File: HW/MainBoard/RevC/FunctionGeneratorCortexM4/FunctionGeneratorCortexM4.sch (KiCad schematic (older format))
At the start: 2 parts, among them J1 Conn_02x05_Odd_Even, J2 Screw_Terminal_01x02

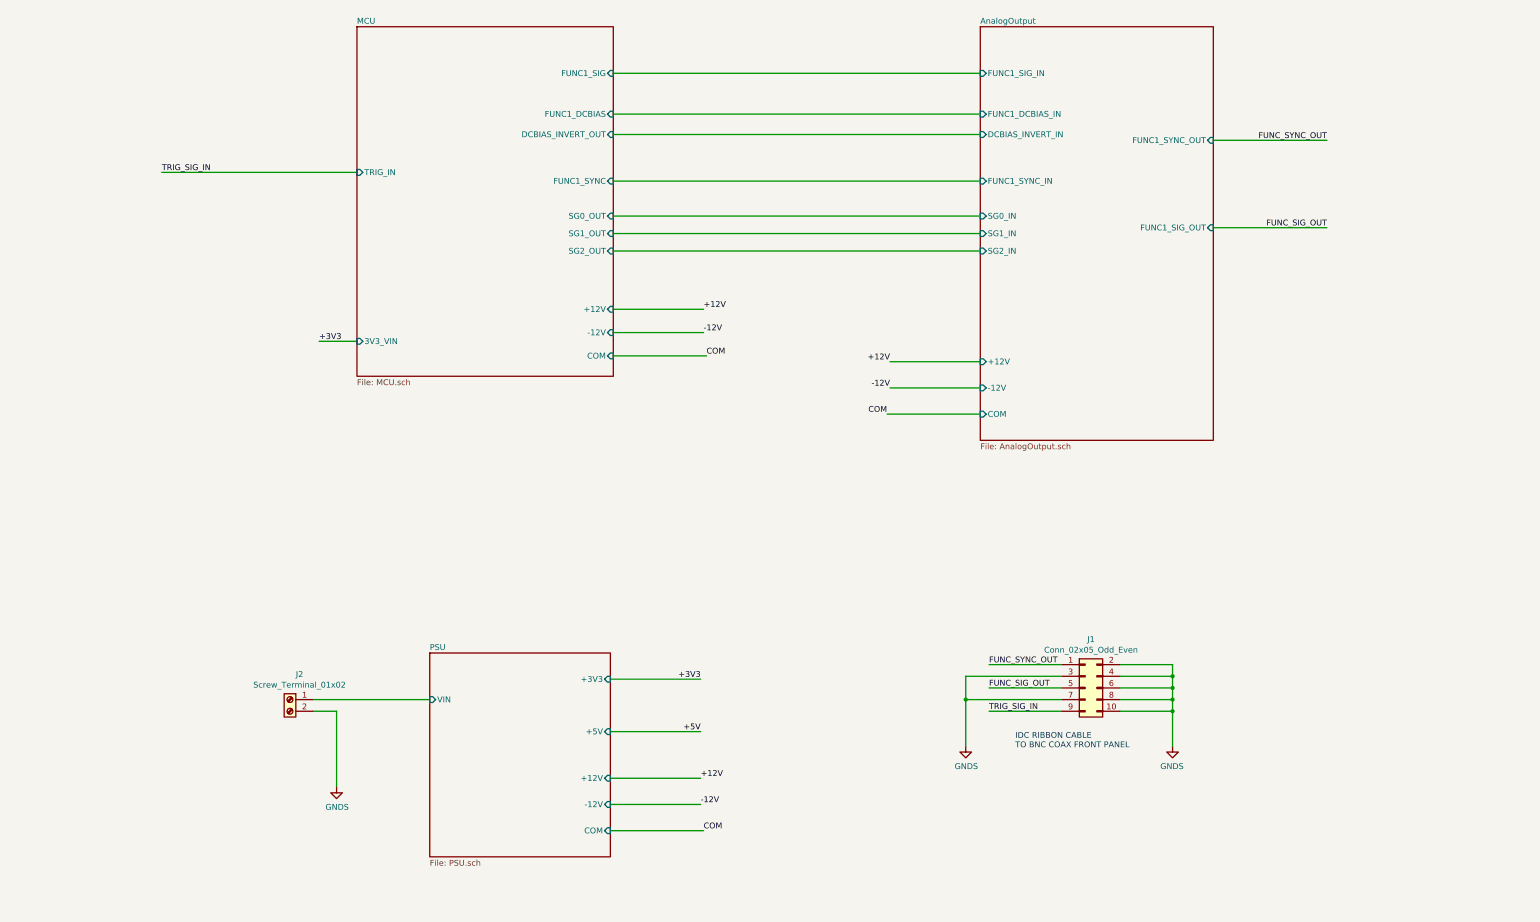
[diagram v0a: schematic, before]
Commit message: Updated MainBoard RevC
- Block diagram and connections completed on schematic
- Need to check MCU pin availability
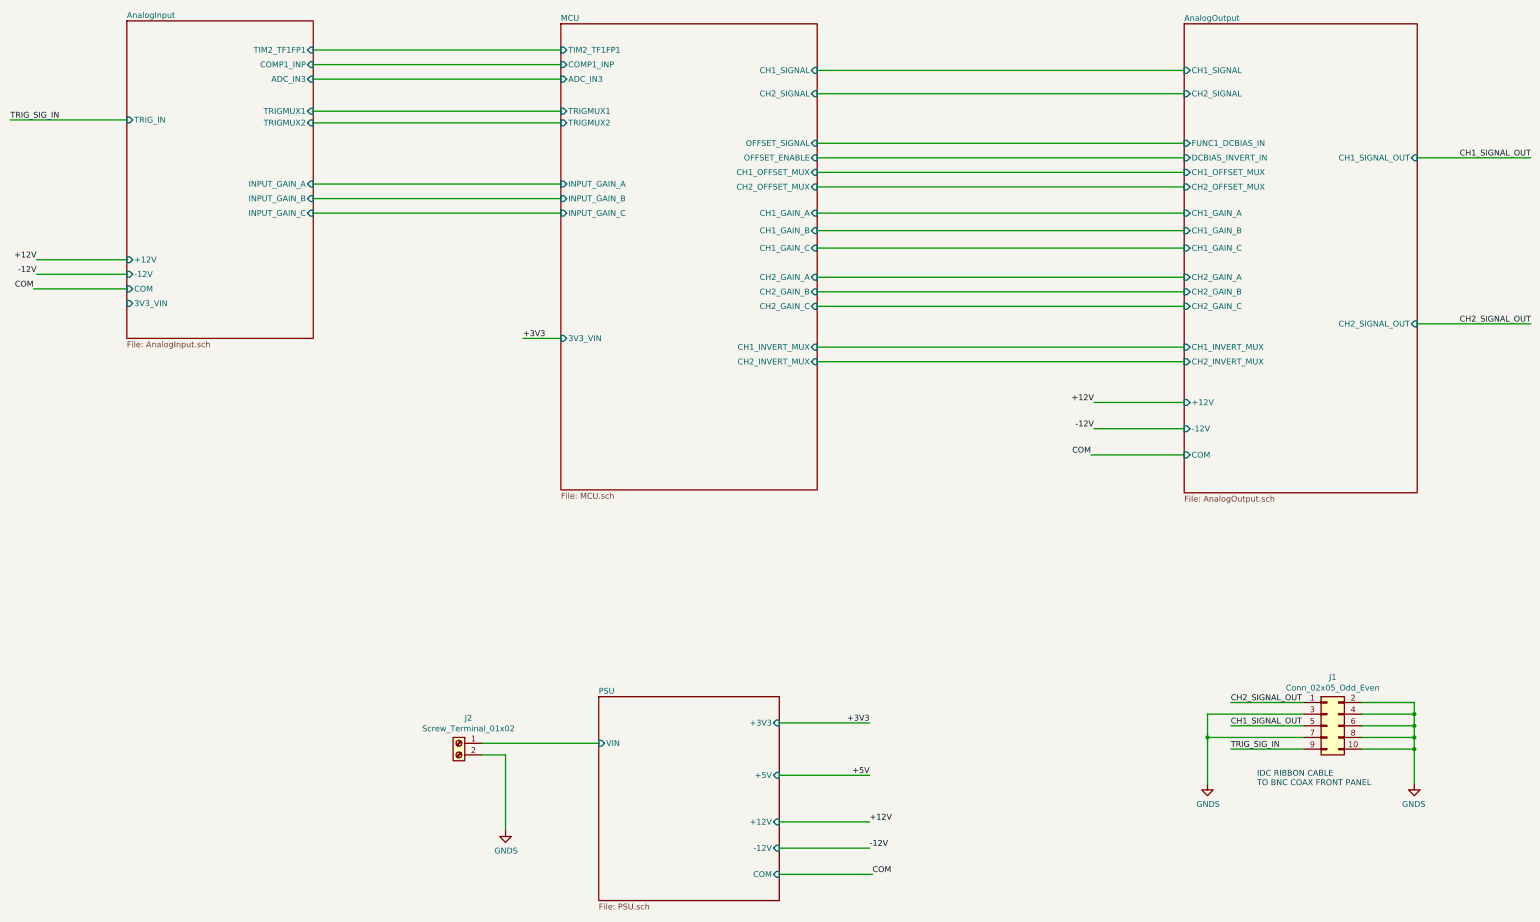
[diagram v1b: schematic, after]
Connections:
- net FUNC_SIG_OUT renamed CH1_SIGNAL_OUT
- net FUNC_SYNC_OUT renamed CH2_SIGNAL_OUT
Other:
- moved on the sheet: J1, J2

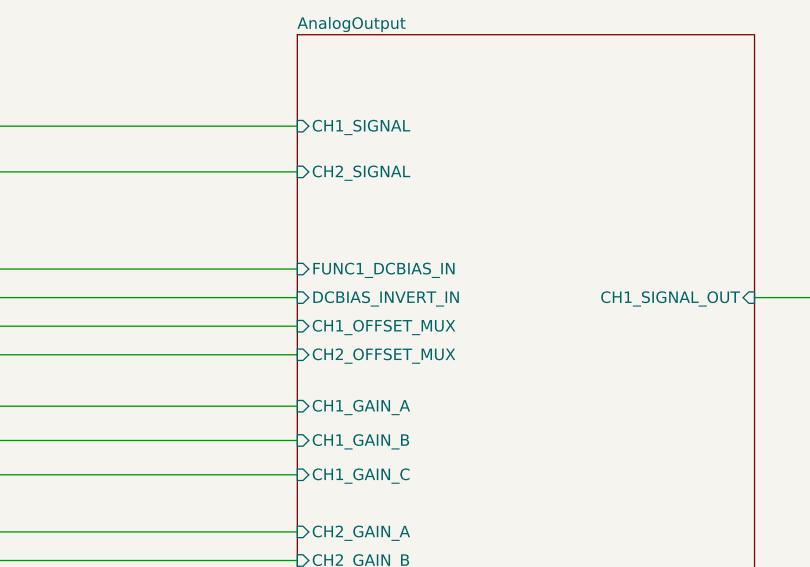
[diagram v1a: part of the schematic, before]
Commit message: Changed OFFSET SPDT to DG470
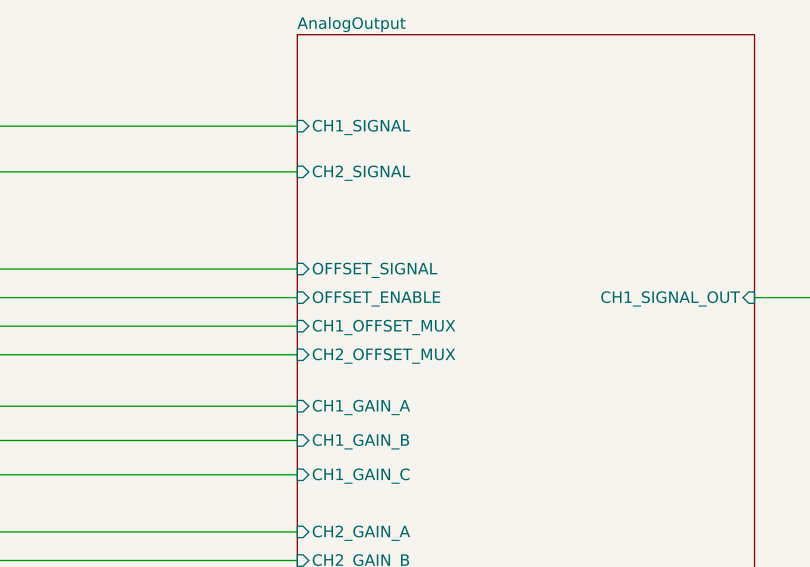
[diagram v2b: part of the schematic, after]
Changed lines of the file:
@@
 F0 "AnalogOutput" 50
 F1 "AnalogOutput.sch" 50
-F2 "FUNC1_DCBIAS_IN" I L 11600 2725 50
-F3 "DCBIAS_INVERT_IN" I L 11600 2850 50
-F4 "+12V" I L 11600 4950 50
-F5 "-12V" I L 11600 5175 50
-F6 "COM" I L 11600 5400 50
-F7 "CH1_GAIN_A" I L 11600 3325 50
-F8 "CH1_GAIN_B" I L 11600 3475 50
-F9 "CH1_GAIN_C" I L 11600 3625 50
-F10 "CH2_GAIN_C" I L 11600 4125 50
-F11 "CH2_GAIN_B" I L 11600 4000 50
-F12 "CH2_GAIN_A" I L 11600 3875 50
-F13 "CH2_SIGNAL" I L 11600 2300 50
-F14 "CH1_SIGNAL" I L 11600 2100 50
-F15 "CH1_OFFSET_MUX" I L 11600 2975 50
-F16 "CH2_OFFSET_MUX" I L 11600 3100 50
-F17 "CH1_INVERT_MUX" I L 11600 4475 50
-F18 "CH2_INVERT_MUX" I L 11600 4600 50
-F19 "CH1_SIGNAL_OUT" I R 13600 2850 50
-F20 "CH2_SIGNAL_OUT" I R 13600 4275 50
+F2 "+12V" I L 11600 4950 50
+F3 "-12V" I L 11600 5175 50
+F4 "COM" I L 11600 5400 50
+F5 "CH1_GAIN_A" I L 11600 3325 50
+F6 "CH1_GAIN_B" I L 11600 3475 50
+F7 "CH1_GAIN_C" I L 11600 3625 50
+F8 "CH2_GAIN_C" I L 11600 4125 50
+F9 "CH2_GAIN_B" I L 11600 4000 50
+F10 "CH2_GAIN_A" I L 11600 3875 50
+F11 "CH2_SIGNAL" I L 11600 2300 50
+F12 "CH1_SIGNAL" I L 11600 2100 50
+F13 "CH1_OFFSET_MUX" I L 11600 2975 50
+F14 "CH2_OFFSET_MUX" I L 11600 3100 50
+F15 "CH1_INVERT_MUX" I L 11600 4475 50
+F16 "CH2_INVERT_MUX" I L 11600 4600 50
+F17 "CH1_SIGNAL_OUT" I R 13600 2850 50
+F18 "CH2_SIGNAL_OUT" I R 13600 4275 50
+F19 "OFFSET_SIGNAL" I L 11600 2725 50
+F20 "OFFSET_ENABLE" I L 11600 2850 50
 $EndSheet
 Wire Wire Line
